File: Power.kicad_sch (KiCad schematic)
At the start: 43 parts, among them J2 S2B-PH-SM4-TB, Q1 DMP3099L, Q2 2N7002, Q3 2N7002, SW4 KMR231NG, SW5 KSS3xxGx, U2 AP2112K-3.3, U3 BQ21040DBV

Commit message: For design review X01-001 Ammendment: Changed ALL VIAS to 0.3/0.55 to reduce fab cost. Signed-off-by: James Mendel <jrm.mendel@gmail.com>
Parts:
- C17, C18, C7, C8: MPN (none) -> CL10B104KO8NNNC
- C3, C4, C5, C6: MPN (none) -> CL10A105KO8NNNC
- R10, R13, R27, R28, R29, R7, R8, R9: MPN (none) -> RC0603FR-07100KL
- R11, R12, R14, R17, R4: MPN (none) -> RC0603FR-0710KL
- R18, R5, R6: MPN (none) -> RC0603FR-071K5L

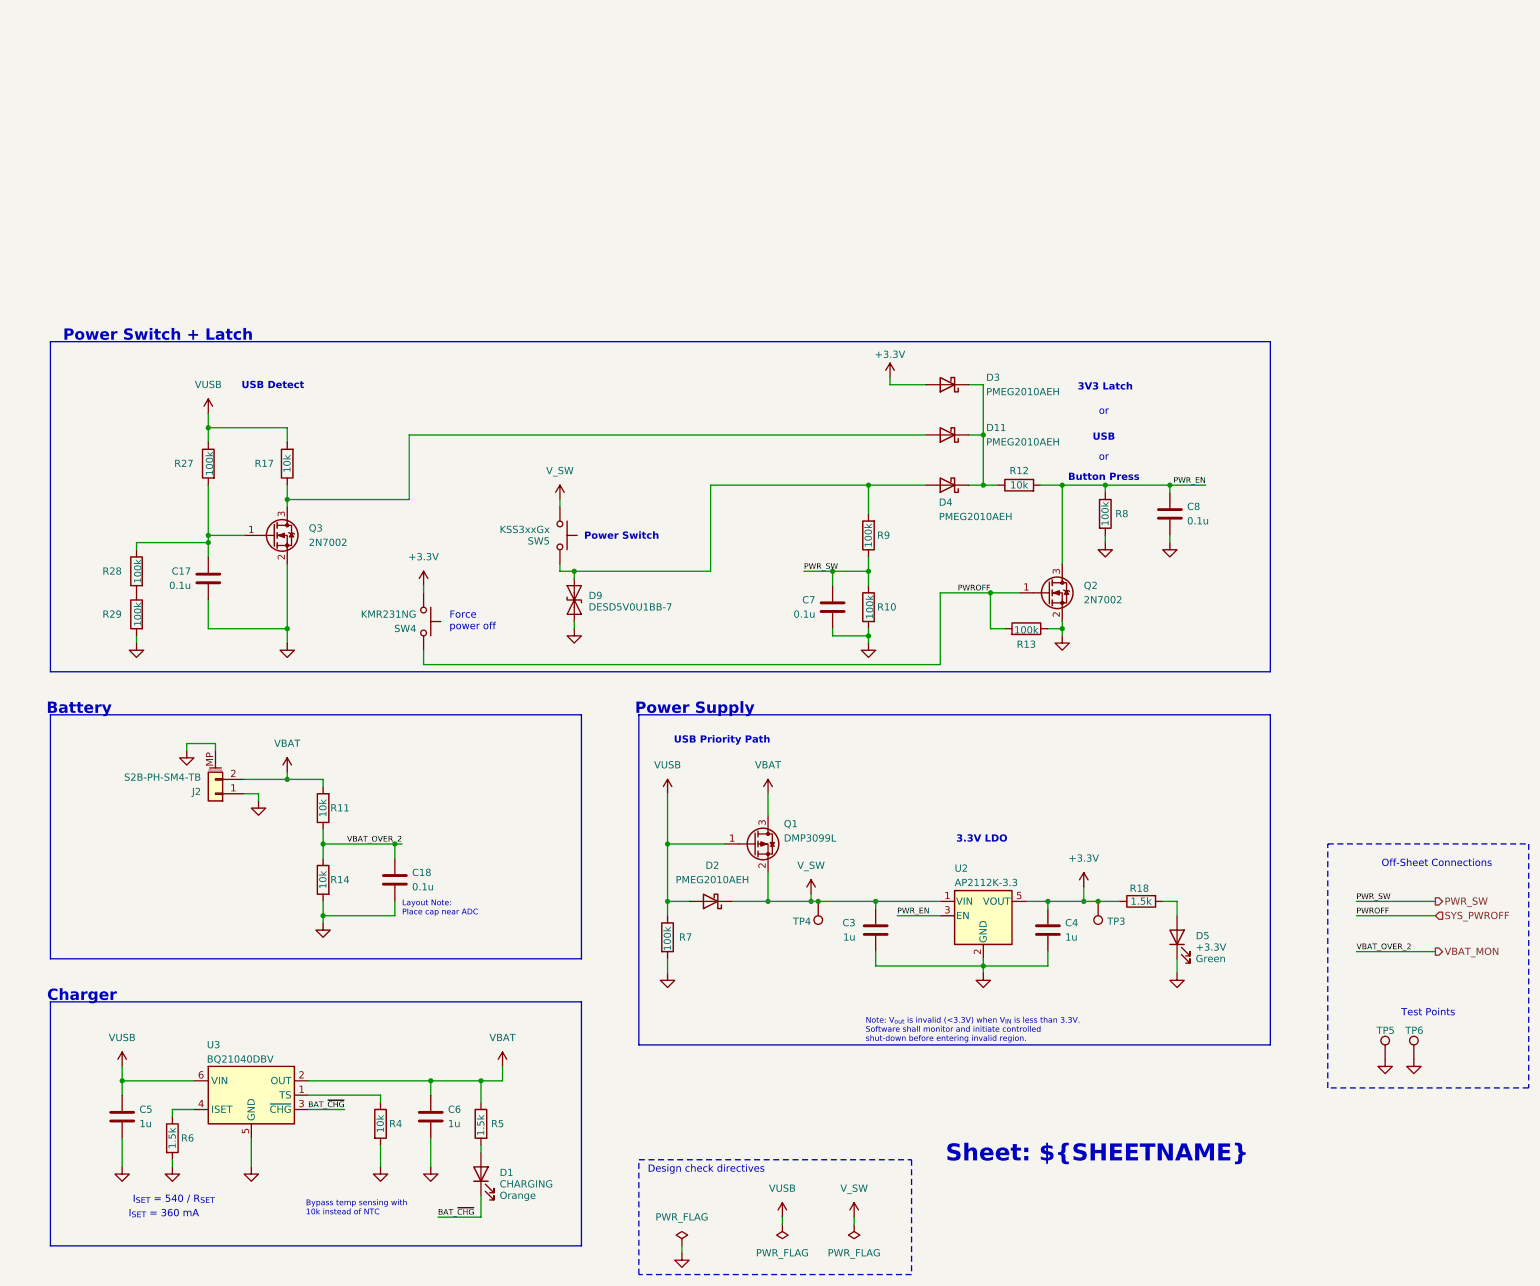
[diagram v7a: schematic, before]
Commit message: Release X01-003 - Added "JRM" logo to L3 and and Modem Works logo to L4. - Upated copyright - Added alternates for some components - Some cleanup on SCH and PCB.
Signed-off-by: James Mendel <jrm.mendel@gmail.com>
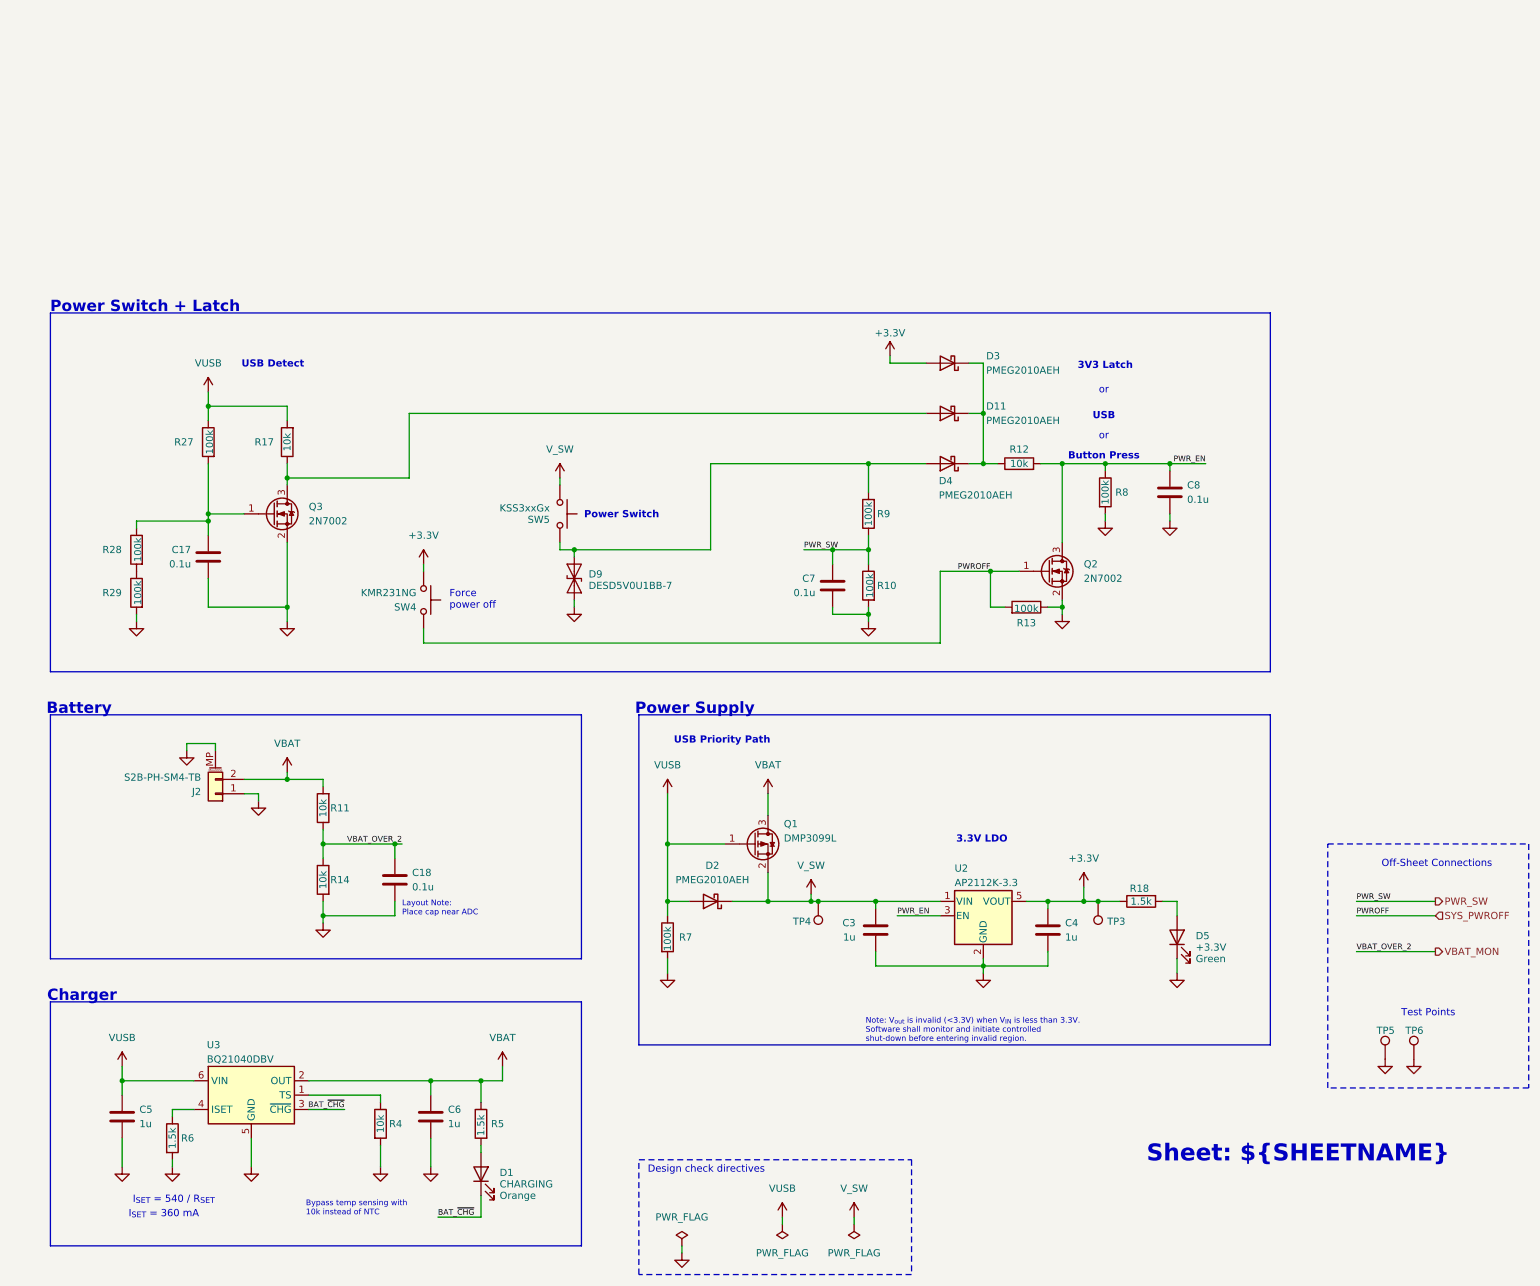
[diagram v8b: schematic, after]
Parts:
- SW5: Alt1 (none) -> KSS322GLFG; Alt2 (none) -> KSS323GLFG; MPN KSS323GLFG -> KSS312GLFG
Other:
- company: J. MENDEL -> ${COMPANY}
- moved on the sheet: C17, C7, C8, D11, D3, D4, D9, Q2, Q3, R10, R12, R13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
